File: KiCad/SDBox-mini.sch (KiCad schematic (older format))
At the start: 2 parts, among them J1 DB25_Male

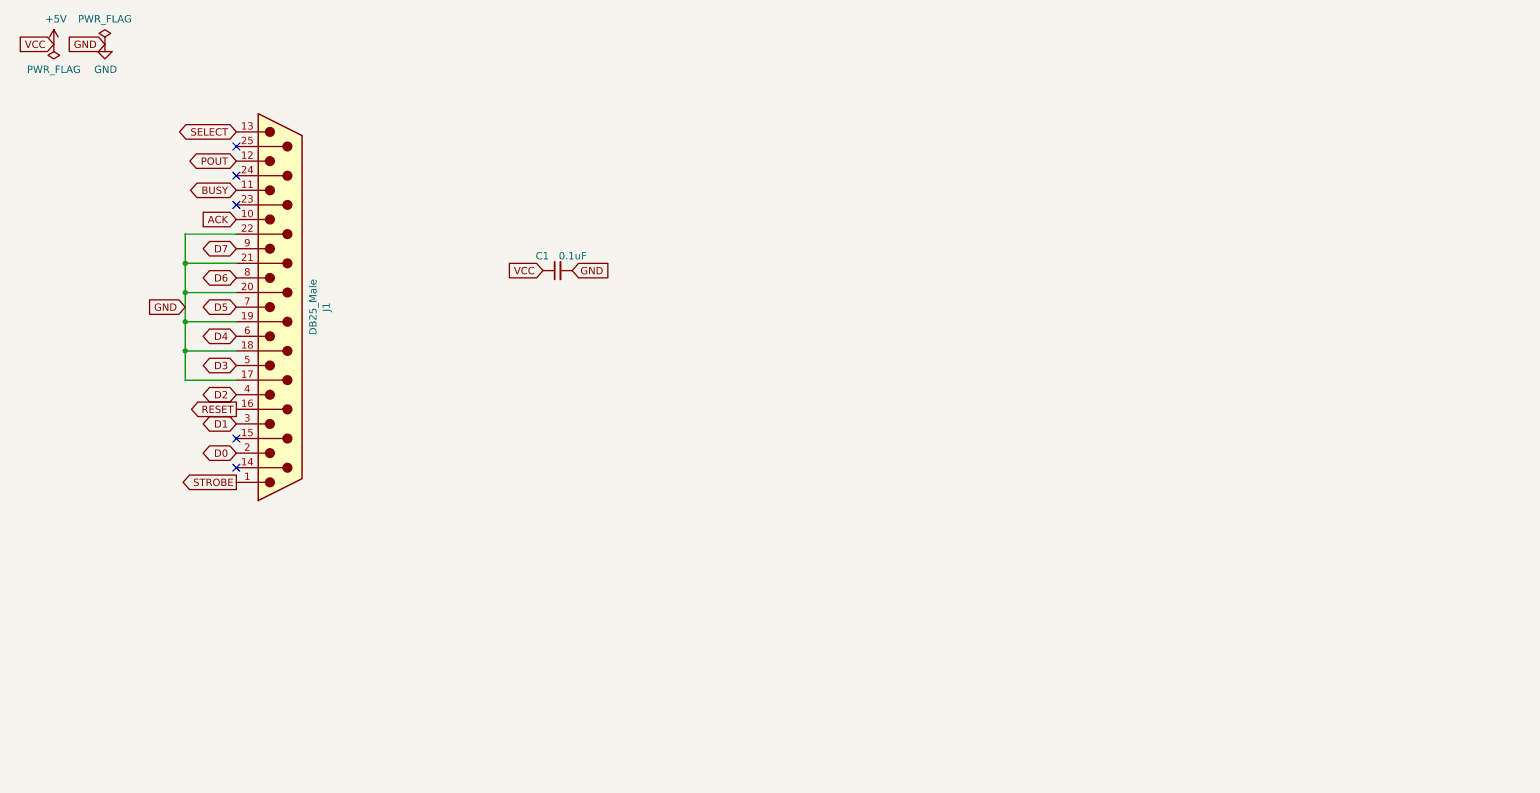
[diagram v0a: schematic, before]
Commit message: resized PCB and added some components
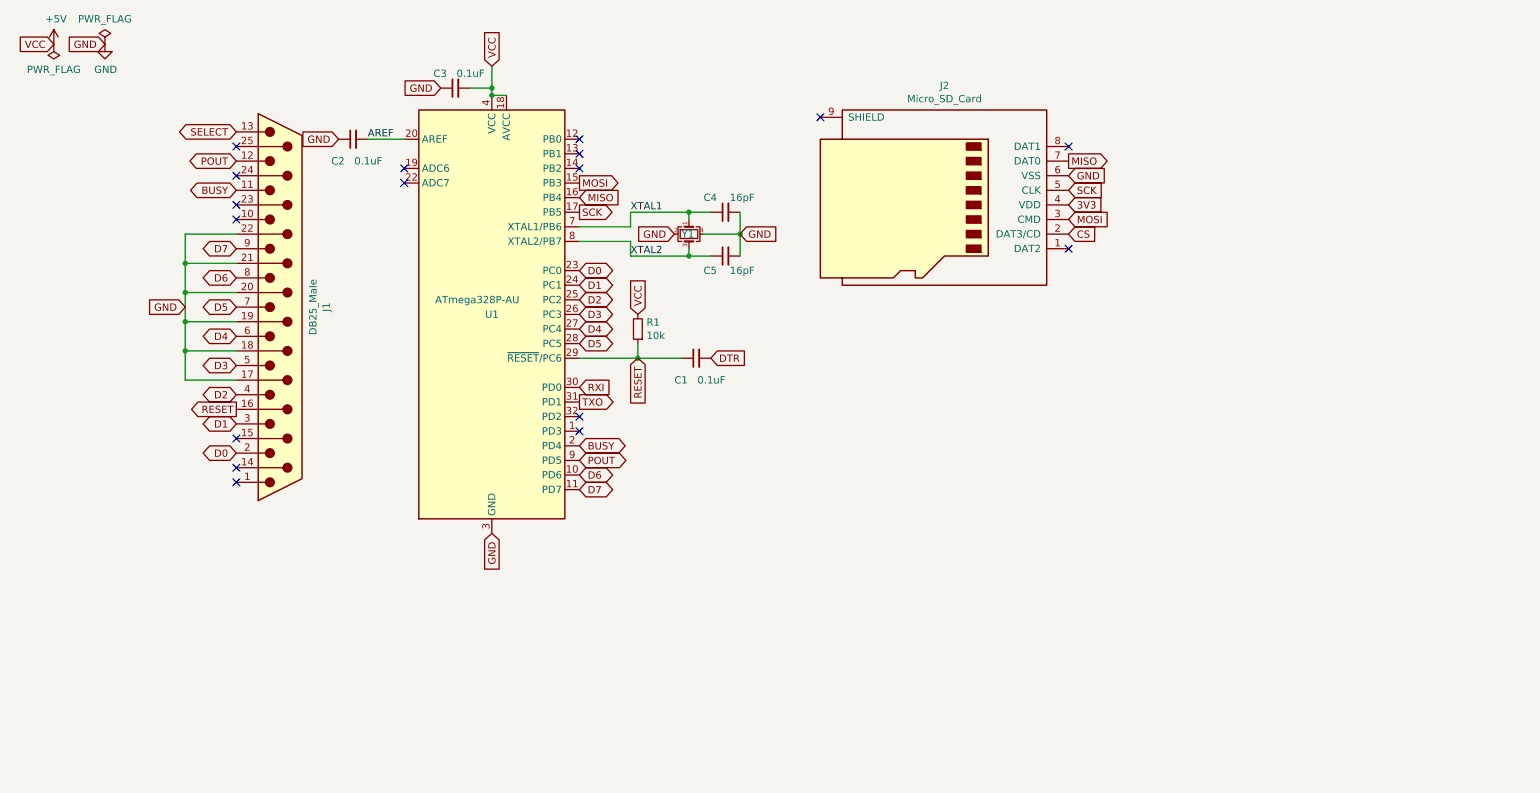
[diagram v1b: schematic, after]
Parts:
- added C1, C3: 0.1uF, Capacitor_SMD:C_0603_1608Metric_Pad1.05x0.95mm_HandSolder, symbol Device:C_Small
- added C4, C5: 16pF, Capacitor_SMD:C_0603_1608Metric_Pad1.05x0.95mm_HandSolder, symbol Device:C_Small
- added J2: Micro_SD_Card, SDBox-mini:GCT-MEM2055-00-190-01-A, symbol Connector:Micro_SD_Card
- added R1: 10k, Resistor_SMD:R_0603_1608Metric_Pad1.05x0.95mm_HandSolder, symbol Device:R_Small
- added U1: ATmega328P-AU, Package_QFP:TQFP-32_7x7mm_P0.8mm, symbol MCU_Microchip_ATmega:ATmega328P-AU
- added Y1: Crystal_GND24_Small, Oscillator:Oscillator_SMD_Fordahl_DFAS15-4Pin_5.0x3.2mm_HandSoldering, symbol Device:Crystal_GND24_Small
- renumbered C1 to C2
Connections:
- net +5V: now also C3.2, R1.2, U1.18 (AVCC), U1.4 (VCC), U1.6 (VCC); no longer C2.1
- net BUSY: now also U1.2 (PD4)
- net D0: now also U1.23 (PC0)
- net D1: now also U1.24 (PC1)
- net D2: now also U1.25 (PC2)
- net D3: now also U1.26 (PC3)
- net D4: now also U1.27 (PC4)
- net D5: now also U1.28 (PC5)
- net D6: now also U1.10 (PD6)
- net D7: now also U1.11 (PD7)
- net GND: now also C2.1, C3.1, C4.2, C5.2, J2.6 (VSS), U1.21 (GND), U1.3 (GND), U1.5 (GND), Y1.2, Y1.4; no longer C2.2
- net POUT: now also U1.9 (PD5)
- net RESET: now also C1.1, R1.1, U1.29 (~RESET~/PC6)
- net ACK: no longer names the net of J1.10
- net STROBE: no longer names the net of J1.1
- new net 3V3: J2.4 (VDD)
- new net AREF: C2.2, U1.20 (AREF)
- new net CS: J2.2 (DAT3/CD)
- new net DTR: C1.2
- new net MISO: J2.7 (DAT0), U1.16 (PB4)
- new net MOSI: J2.3 (CMD), U1.15 (PB3)
- new net RXI: U1.30 (PD0)
- new net SCK: J2.5 (CLK), U1.17 (PB5)
- new net TXO: U1.31 (PD1)
- new net XTAL1: C4.1, U1.7 (XTAL1/PB6), Y1.1
- new net XTAL2: C5.1, U1.8 (XTAL2/PB7), Y1.3
- no-connect marks 5 -> 17
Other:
- moved on the sheet: C2
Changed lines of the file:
@@
 $EndDescr
 $Comp
-L Device:C_Small C1
+L Device:C_Small C2
 U 1 1 606A3110
-P 4400 2500
-F 0 "C1" V 4500 2650 50  0000 R CNN
-F 1 "0.1uF" V 4500 2300 50  0000 L CNN
-F 2 "Capacitor_SMD:C_0603_1608Metric_Pad1.05x0.95mm_HandSolder" H 4400 2500 50  0001 C CNN
-F 3 "~" H 4400 2500 50  0001 C CNN
-	1    4400 2500
-	0    -1   -1   0
-$EndComp
-Text GLabel 4500 2500 2    50   Input ~ 0
-GND
-Text GLabel 4300 2500 0    50   Input ~ 0
-VCC
+P 3000 1600
+F 0 "C2" V 2850 1750 50  0000 R CNN
+F 1 "0.1uF" V 2850 1400 50  0000 L CNN
+F 2 "Capacitor_SMD:C_0603_1608Metric_Pad1.05x0.95mm_HandSolder" H 3000 1600 50  0001 C CNN
+F 3 "~" H 3000 1600 50  0001 C CNN
+	1    3000 1600
+	0    -1   -1   0
+$EndComp
+Text GLabel 2900 1600 0    50   Input ~ 0
+GND
 Text GLabel 950  950  0    50   Input ~ 0
 VCC
@@
 Text GLabel 2200 1950 0    50   BiDi ~ 0
 BUSY
-Text GLabel 2200 2150 0    50   Input ~ 0
-ACK
 Text GLabel 1850 2750 0    50   Input ~ 0
 GND
@@
 Text GLabel 2200 3750 0    50   BiDi ~ 0
 D0
+$Comp
+L MCU_Microchip_ATmega:ATmega328P-AU U1
+U 1 1 60F7C9EE
+P 3950 2800
+F 0 "U1" H 3950 2800 50  0000 C CNN
+F 1 "ATmega328P-AU" H 3850 2900 50  0000 C CNN
+F 2 "Package_QFP:TQFP-32_7x7mm_P0.8mm" H 3950 2800 50  0001 C CIN
+F 3 "http://ww1.microchip.com/downloads/en/DeviceDoc/ATmega328_P%20AVR%20MCU%20with%20picoPower%20Technology%20Data%20Sheet%2040001984A.pdf" H 3950 2800 50  0001 C CNN
+	1    3950 2800
+	1    0    0    -1
+$EndComp
+Text GLabel 4550 2500 2    50   BiDi ~ 0
+D0
+Text GLabel 4550 2600 2    50   BiDi ~ 0
+D1
+Text GLabel 4550 2700 2    50   BiDi ~ 0
+D2
+Text GLabel 4550 2800 2    50   BiDi ~ 0
+D3
+Text GLabel 4550 2900 2    50   BiDi ~ 0
+D4
+Text GLabel 4550 3000 2    50   BiDi ~ 0
+D5
+Text GLabel 4550 3900 2    50   BiDi ~ 0
+D6
+Text GLabel 4550 4000 2    50   BiDi ~ 0
+D7
+NoConn ~ 3350 1800
+NoConn ~ 3350 1900
+Text GLabel 3950 4300 3    50   Input ~ 0
+GND
+Text GLabel 3950 1100 1    50   Input ~ 0
+VCC
+Wire Wire Line
+	3950 1300 4050 1300
+$Comp
+L Device:R_Small R1
+U 1 1 60F84B00
+P 4950 2900
+F 0 "R1" H 4891 2854 50  0000 R CNN
+F 1 "10k" H 4891 2945 50  0000 R CNN
+F 2 "Resistor_SMD:R_0603_1608Metric_Pad1.05x0.95mm_HandSolder" H 4950 2900 50  0001 C CNN
+F 3 "~" H 4950 2900 50  0001 C CNN
+	1    4950 2900
+	-1   0    0    1
+$EndComp
 NoConn ~ 2200 3850
-Text GLabel 2200 3950 0    50   Output ~ 0
-STROBE
+Text GLabel 4950 2800 1    50   Input ~ 0
+VCC
+Text Label 3100 1600 0    50   ~ 0
+AREF
+Wire Wire Line
+	3100 1600 3350 1600
+Wire Wire Line
+	4550 3100 4950 3100
+Wire Wire Line
+	4950 3000 4950 3100
+Text GLabel 5200 2250 0    50   Input ~ 0
+GND
+$Comp
+L Device:Crystal_GND24_Small Y1
+U 1 1 60F9A65B
+P 5300 2250
+F 0 "Y1" V 5300 2200 50  0000 L CNN
+F 1 "Crystal_GND24_Small" V 5500 2400 50  0001 L CNN
+F 2 "Oscillator:Oscillator_SMD_Fordahl_DFAS15-4Pin_5.0x3.2mm_HandSoldering" H 5300 2250 50  0001 C CNN
+F 3 "~" H 5300 2250 50  0001 C CNN
+	1    5300 2250
+	0    1    1    0
+$EndComp
+Text GLabel 5650 2250 2    50   Input ~ 0
+GND
+$Comp
+L Device:C_Small C4
+U 1 1 60FA06FB
+P 5550 2100
+F 0 "C4" V 5650 2250 50  0000 R CNN
+F 1 "16pF" V 5650 1900 50  0000 L CNN
+F 2 "Capacitor_SMD:C_0603_1608Metric_Pad1.05x0.95mm_HandSolder" H 5550 2100 50  0001 C CNN
+F 3 "~" H 5550 2100 50  0001 C CNN
+	1    5550 2100
+	0    -1   -1   0
+$EndComp
+Wire Wire Line
+	4900 2100 5300 2100
+$Comp
+L Device:C_Small C5
+U 1 1 60FA5116
+P 5550 2400
+F 0 "C5" V 5450 2550 50  0000 R CNN
+F 1 "16pF" V 5450 2200 50  0000 L CNN
+F 2 "Capacitor_SMD:C_0603_1608Metric_Pad1.05x0.95mm_HandSolder" H 5550 2400 50  0001 C CNN
+F 3 "~" H 5550 2400 50  0001 C CNN
+	1    5550 2400
+	0    -1   -1   0
+$EndComp
+Wire Wire Line
+	5400 2250 5650 2250
+Connection ~ 5650 2250
+$Comp
+L Device:C_Small C3
+U 1 1 60FA7C64
+P 3700 1250
+F 0 "C3" V 3800 1400 50  0000 R CNN
+F 1 "0.1uF" V 3800 1050 50  0000 L CNN
+F 2 "Capacitor_SMD:C_0603_1608Metric_Pad1.05x0.95mm_HandSolder" H 3700 1250 50  0001 C CNN
+F 3 "~" H 3700 1250 50  0001 C CNN
+	1    3700 1250
+	0    -1   -1   0
+$EndComp
+Wire Wire Line
+	3950 1100 3950 1250
+Connection ~ 3950 1300
+Wire Wire Line
+	3800 1250 3950 1250
+Connection ~ 3950 1250
+Wire Wire Line
+	3950 1250 3950 1300
+Text GLabel 3600 1250 0    50   Input ~ 0
+GND
+Text Label 4900 2100 0    50   ~ 0
+XTAL1
+Text Label 4900 2400 0    50   ~ 0
+XTAL2
+Wire Wire Line
+	4900 2400 5300 2400
+Wire Wire Line
+	5300 2350 5300 2400
+Connection ~ 5300 2400
+Wire Wire Line
+	5300 2400 5450 2400
+Wire Wire Line
+	5300 2150 5300 2100
+Wire Wire Line
+	5300 2100 5450 2100
+Connection ~ 5300 2100
+Wire Wire Line
+	5650 2100 5650 2250
+Wire Wire Line
+	5650 2250 5650 2400
+Text GLabel 4550 3800 2    50   BiDi ~ 0
+POUT
+Text GLabel 4550 3700 2    50   BiDi ~ 0
+BUSY
+NoConn ~ 4550 3500
+NoConn ~ 4550 3600
+Text GLabel 4550 3300 2    50   Input ~ 0
+RXI
+Text GLabel 4550 3400 2    50   Output ~ 0
+TXO
+NoConn ~ 2200 2150
+NoConn ~ 2200 3950
+Text GLabel 4550 2000 2    50   Input ~ 0
+MISO
+Text GLabel 4550 1900 2    50   Output ~ 0
+MOSI
+Text GLabel 4550 2100 2    50   Output ~ 0
+SCK
+Wire Wire Line
+	4900 2200 4900 2100
+Wire Wire Line
+	4550 2200 4900 2200
+Wire Wire Line
+	4900 2300 4900 2400
+Wire Wire Line
+	4550 2300 4900 2300
+Text GLabel 5450 3100 2    50   Input ~ 0
+DTR
+$Comp
+L Device:C_Small C1
+U 1 1 60F8E9CC
+P 5350 3100
+F 0 "C1" V 5200 3250 50  0000 R CNN
+F 1 "0.1uF" V 5200 2900 50  0000 L CNN
+F 2 "Capacitor_SMD:C_0603_1608Metric_Pad1.05x0.95mm_HandSolder" H 5350 3100 50  0001 C CNN
+F 3 "~" H 5350 3100 50  0001 C CNN
+	1    5350 3100
+	0    -1   -1   0
+$EndComp
+Text GLabel 4950 3100 3    50   Input ~ 0
+RESET
+Wire Wire Line
+	4950 3100 5250 3100
+Connection ~ 4950 3100
+NoConn ~ 4550 1600
+NoConn ~ 4550 1700
+NoConn ~ 4550 1800
+$Comp
+L Connector:Micro_SD_Card J2
+U 1 1 60FD5546
+P 7000 2050
+F 0 "J2" H 6950 1233 50  0000 C CNN
+F 1 "Micro_SD_Card" H 6950 1324 50  0000 C CNN
+F 2 "SDBox-mini:GCT-MEM2055-00-190-01-A" H 8150 2350 50  0001 C CNN
+F 3 "http://katalog.we-online.de/em/datasheet/693072010801.pdf" H 7000 2050 50  0001 C CNN
+	1    7000 2050
+	-1   0    0    1
+$EndComp
+NoConn ~ 7900 2350
+Text GLabel 7900 1750 2    50   Output ~ 0
+MISO
+Text GLabel 7900 1850 2    50   Input ~ 0
+GND
+Text GLabel 7900 1950 2    50   Input ~ 0
+SCK
+Text GLabel 7900 2050 2    50   Input ~ 0
+3V3
+Text GLabel 7900 2150 2    50   Input ~ 0
+MOSI
+NoConn ~ 7900 1650
+NoConn ~ 6200 1450
+Text GLabel 7900 2250 2    50   Input ~ 0
+CS
 $EndSCHEMATC
